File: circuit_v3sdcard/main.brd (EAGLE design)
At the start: 21.7 x 29.5 mm, 18 parts, among them CN1 SD, CN3 MICROSD, CN4 5035481020, IC1 C8051F381-GM, IC3 N25Q512A, IC4 KC2016K, IC6 MPU-9250

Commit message: Fix parts positions
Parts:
- added C1: 1.0u, reg,cap:1005
- added R3: 100, reg,cap:1005
- moved IC1 36.7 mm to (4.96, 20.1)
- moved C6 36.4 mm to (0.62, 19.6), turned to 270 degrees
- moved C9 15.4 mm to (16.6, 23.3), turned to 0 degrees
- moved D4 13.1 mm to (1.82, 13.8)
- moved C3 12.3 mm to (5.83, 13.4)
- moved C2 12.3 mm to (8.33, 13.4)
- moved C4 12.3 mm to (4.33, 12.6)
- moved IC6 12.3 mm to (6.83, 10.1)
- moved R26 11.0 mm to (14.1, 23.3), turned to 180 degrees
- moved R2 9.85 mm to (3.51, 6.00)
- moved IC3 8.15 mm to (13.6, 19.8), turned to 0 degrees
- moved C10 2.18 mm to (19.8, 21.7), turned to 0 degrees
- moved IC4 1.78 mm to (19.7, 19.1)
- moved R1 1.67 mm to (7.44, 1.29), turned to 90 degrees
- moved D3 0.55 mm to (1.61, 9.61)
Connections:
- new net N$4: IC1.8, R3.P$1
- net DGND: now also C1.P$1
- net N$1: now also C1.P$2
- net VBUS: now also R3.P$2; no longer IC1.8
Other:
- outline, holes or cut-outs redrawn

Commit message: Added wiring
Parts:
- moved C2 6.15 mm to (4.92, 8.24), turned to 0 degrees
- moved C4 6.03 mm to (9.05, 8.81), turned to 90 degrees
- moved C3 5.93 mm to (7.74, 7.75), turned to 180 degrees
- moved C6 3.42 mm to (2.29, 16.6), turned to 90 degrees
- moved R1 2.72 mm to (7.43, 4.00)
- moved IC6 1.50 mm to (6.83, 11.6), turned to 0 degrees
- moved C1 1.19 mm to (1.28, 16.6)
- moved R2 0.46 mm to (3.05, 5.96)
- moved C9 0.13 mm to (16.7, 23.3)
- moved R26 0.13 mm to (14.2, 23.3), turned to 0 degrees
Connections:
- net D+: now also CN4.4; no longer CN4.6
- net D-: now also CN4.6; no longer CN4.4
- net GPIO0: now also IC1.12; no longer IC1.26
- net GPIO1: now also IC1.11; no longer IC1.25
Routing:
- net DGND: track 1.98 -> 132.2 mm, vias 0 -> 19
- net +3V3: track 1.54 -> 68.3 mm, vias 0 -> 9
- net N$11: track 0.00 -> 34.2 mm, vias 0 -> 2
- net D+: track 0.00 -> 31.9 mm
- net TX1: track 0.00 -> 31.6 mm, vias 0 -> 2
- net RX1: track 0.00 -> 31.3 mm, vias 0 -> 2
- net D-: track 0.00 -> 30.5 mm
- net N$2: track 0.00 -> 28.6 mm, vias 0 -> 1
- net N$14: track 0.00 -> 27.1 mm, vias 0 -> 1
- net EEPROM_MOSI: track 0.00 -> 26.5 mm
- net EEPROM_SCK: track 0.00 -> 26.3 mm
- net C2D: track 0.00 -> 23.4 mm, vias 0 -> 2
- net C2CK: track 0.00 -> 23.3 mm, vias 0 -> 3
- net N$3: track 0.00 -> 21.4 mm, vias 0 -> 1
- net GPIO1: track 0.00 -> 20.6 mm, vias 0 -> 1
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
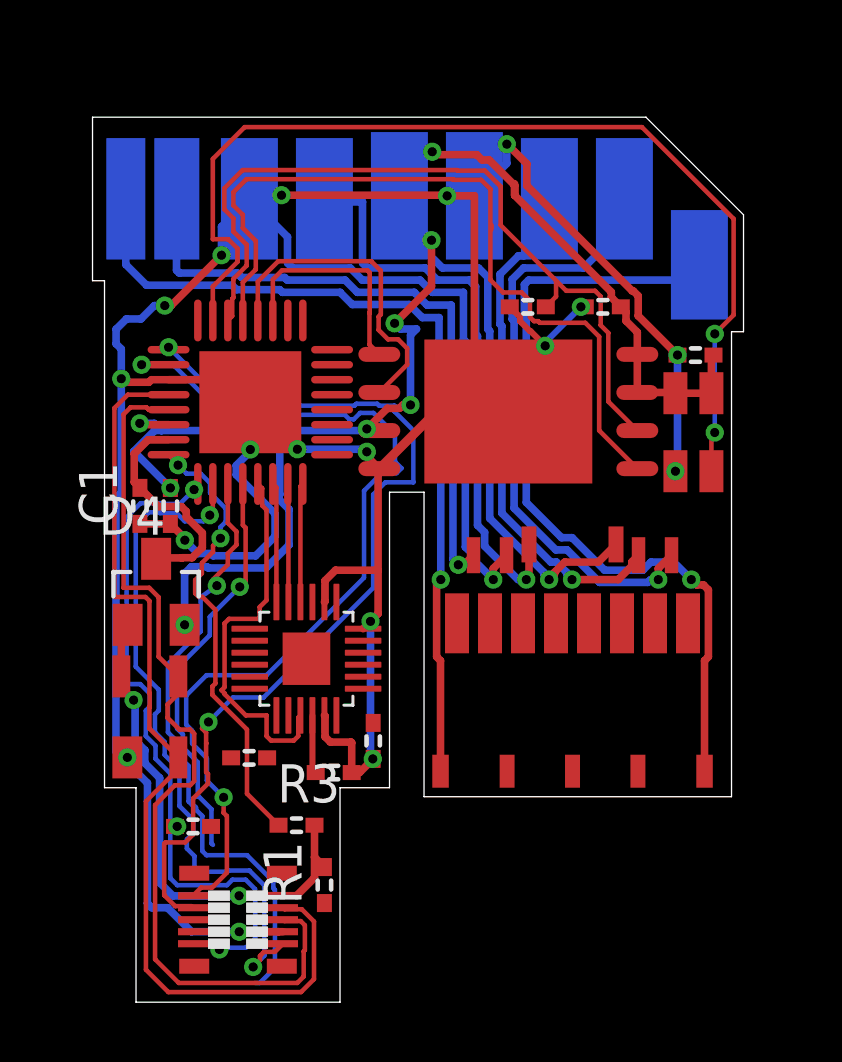
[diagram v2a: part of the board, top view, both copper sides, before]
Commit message: Connected air wires
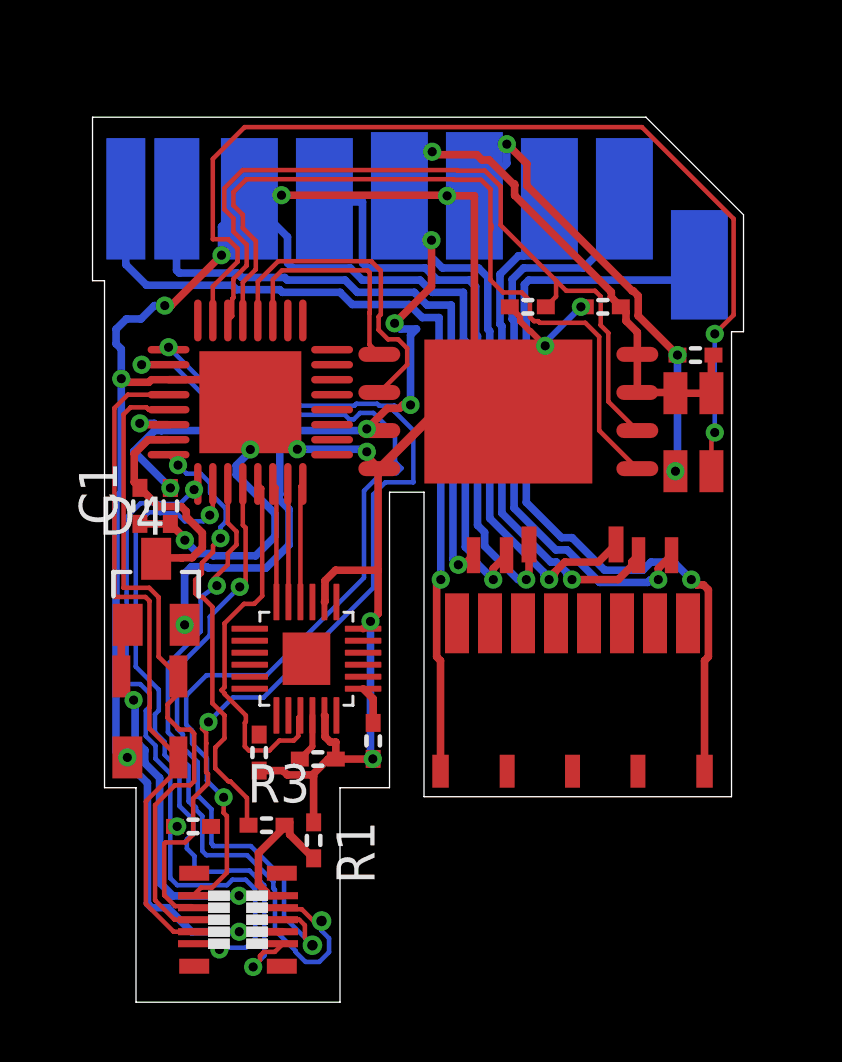
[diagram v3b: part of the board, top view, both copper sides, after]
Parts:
- moved R1 1.53 mm to (7.07, 5.50), turned to 270 degrees
- moved R3 1.00 mm to (5.50, 6.00)
- moved C3 0.70 mm to (7.21, 8.21)
- moved C2 0.38 mm to (5.25, 8.42), turned to 90 degrees
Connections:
- net D+: now also CN4.7; no longer CN4.4
- net D-: now also CN4.5; no longer CN4.6
- net GPIO0: now also CN4.6; no longer CN4.5
- net GPIO1: now also CN4.4; no longer CN4.7
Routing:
- net D+: track 31.9 -> 22.4 mm
- net D-: track 30.5 -> 22.2 mm
- net GPIO0: track 13.5 -> 20.6 mm, vias 1 -> 2
- net GPIO1: track 20.6 -> 23.5 mm, vias 1 -> 2
- net DGND: track 132.2 -> 135.0 mm
- net +3V3: track 68.3 -> 69.5 mm
- net VBUS: track 17.1 -> 18.1 mm

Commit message: Modified circuit
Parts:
- moved C2 0.50 mm to (4.75, 8.42)
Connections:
- net D+: now also CN4.5; no longer CN4.7
- net D-: now also CN4.3; no longer CN4.5
- net DGND: now also CN4.7; no longer CN4.8
- net GPIO0: now also CN4.8; no longer CN4.6
- net GPIO1: now also CN4.6; no longer CN4.4
- net RX1: now also CN4.4; no longer CN4.3
- net TX1: now also CN4.2; no longer CN4.1
- net VBUS: now also CN4.1; no longer CN4.2
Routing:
- net +3V3: track 69.5 -> 61.9 mm
- net DGND: track 135.0 -> 128.3 mm
- net C2D: track 23.4 -> 17.4 mm
- net N$4: track 14.9 -> 20.6 mm
- net TX1: track 31.6 -> 28.5 mm
- net RX1: track 31.3 -> 29.3 mm
- net GPIO1: track 23.5 -> 25.4 mm
- net GPIO0: track 20.6 -> 22.2 mm
- net VBUS: track 18.1 -> 17.6 mm
- net IMU_MISO: track 12.7 -> 13.2 mm, vias 0 -> 2

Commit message: No air wire
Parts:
- moved C4 0.57 mm to (8.59, 9.13)
- moved C2 0.50 mm to (4.75, 8.92)
- moved IC6 0.50 mm to (6.83, 12.1)
- moved R3 0.25 mm to (5.55, 6.25), turned to 180 degrees
- moved C3 0.13 mm to (7.14, 8.31)
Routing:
- net +3V3: track 61.9 -> 88.0 mm, vias 9 -> 10
- net N$4: track 20.6 -> 17.7 mm
- net C2D: track 17.4 -> 19.6 mm
- net DGND: track 128.3 -> 126.6 mm
- net RX1: track 29.3 -> 27.6 mm
- net IMU_MISO: track 13.2 -> 12.1 mm
- net TX1: track 28.5 -> 27.5 mm
- net C2CK: track 23.3 -> 22.4 mm, vias 3 -> 4
- net IMU_SCK: track 3.94 -> 3.44 mm
- net IMU_MOSI: track 3.98 -> 3.48 mm
- net IMU_!CS: track 3.97 -> 3.47 mm
- removed copper zone on layer 1, net +3V3

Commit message: Modified circuit
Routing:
- net GPIO1: track 24.9 -> 22.1 mm
- net GPIO0: track 22.2 -> 19.7 mm
- net N$4: track 17.7 -> 15.3 mm
- net N$11: track 34.2 -> 32.1 mm
- net +3V3: track 88.0 -> 86.4 mm
- net EEPROM_MOSI: track 26.3 -> 25.2 mm
- net EEPROM_SCK: track 26.3 -> 25.1 mm
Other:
- board text added: "Yoshiaki Sato"
- board text added: "virtualGimbal v3"
- board text removed: "Y. Sato"
- board text removed: "virtualGimbal"

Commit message: Modified parts values
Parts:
- D4: value HSMS-2854 -> BAT54CL
- IC3: value N25Q512A -> MT29F2G01ABAGDWB
- IC4: value KC2016K -> KC2016K48.0000C1GE00
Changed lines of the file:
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@@
 <layer number="21" name="tPlace" color="7" fill="1" visible="yes" active="yes"/>
 <layer number="22" name="bPlace" color="7" fill="1" visible="yes" active="yes"/>
-<layer number="23" name="tOrigins" color="15" fill="1" visible="no" active="yes"/>
-<layer number="24" name="bOrigins" color="15" fill="1" visible="no" active="yes"/>
+<layer number="23" name="tOrigins" color="15" fill="1" visible="yes" active="yes"/>
+<layer number="24" name="bOrigins" color="15" fill="1" visible="yes" active="yes"/>
 <layer number="25" name="tNames" color="7" fill="1" visible="no" active="yes"/>
 <layer number="26" name="bNames" color="7" fill="1" visible="no" active="yes"/>
@@
 <attribute name="VALUE" x="4.2001" y="16.0064" size="1.27" layer="27" rot="R90"/>
 </element>
-<element name="IC3" library="EEPROM" package="V-PDFN-8" value="N25Q512A" x="13.56" y="19.79">
+<element name="IC3" library="EEPROM" package="V-PDFN-8" value="MT29F2G01ABAGDWB" x="13.56" y="19.79">
 <attribute name="VALUE" x="9.925" y="15.79" size="0.8128" layer="27"/>
 </element>
@@
 <attribute name="VALUE" x="16.075" y="21.375" size="1.27" layer="27"/>
 </element>
-<element name="IC4" library="Oscillator" package="KC2016K" value="KC2016K" x="19.73" y="19.1" rot="R270">
+<element name="IC4" library="Oscillator" package="KC2016K" value="KC2016K48.0000C1GE00" x="19.73" y="19.1" rot="R270">
 <attribute name="VALUE" x="17.252" y="15.452" size="1.27" layer="27" ratio="10"/>
 </element>
@@
 <attribute name="VALUE" x="5.165" y="6.13" size="1.27" layer="27" rot="R270"/>
 </element>
-<element name="D4" library="avago" library_urn="urn:adsk.eagle:library:107" package="SOT23" package3d_urn="urn:adsk.eagle:package:4488/1" value="HSMS-2854" x="1.82" y="13.78">
+<element name="D4" library="avago" library_urn="urn:adsk.eagle:library:107" package="SOT23" package3d_urn="urn:adsk.eagle:package:4488/1" value="BAT54CL" x="1.82" y="13.78">
 <attribute name="NAME" x="-0.085" y="15.685" size="1.27" layer="25"/>
 <attribute name="VALUE" x="-0.085" y="10.605" size="1.27" layer="27"/>

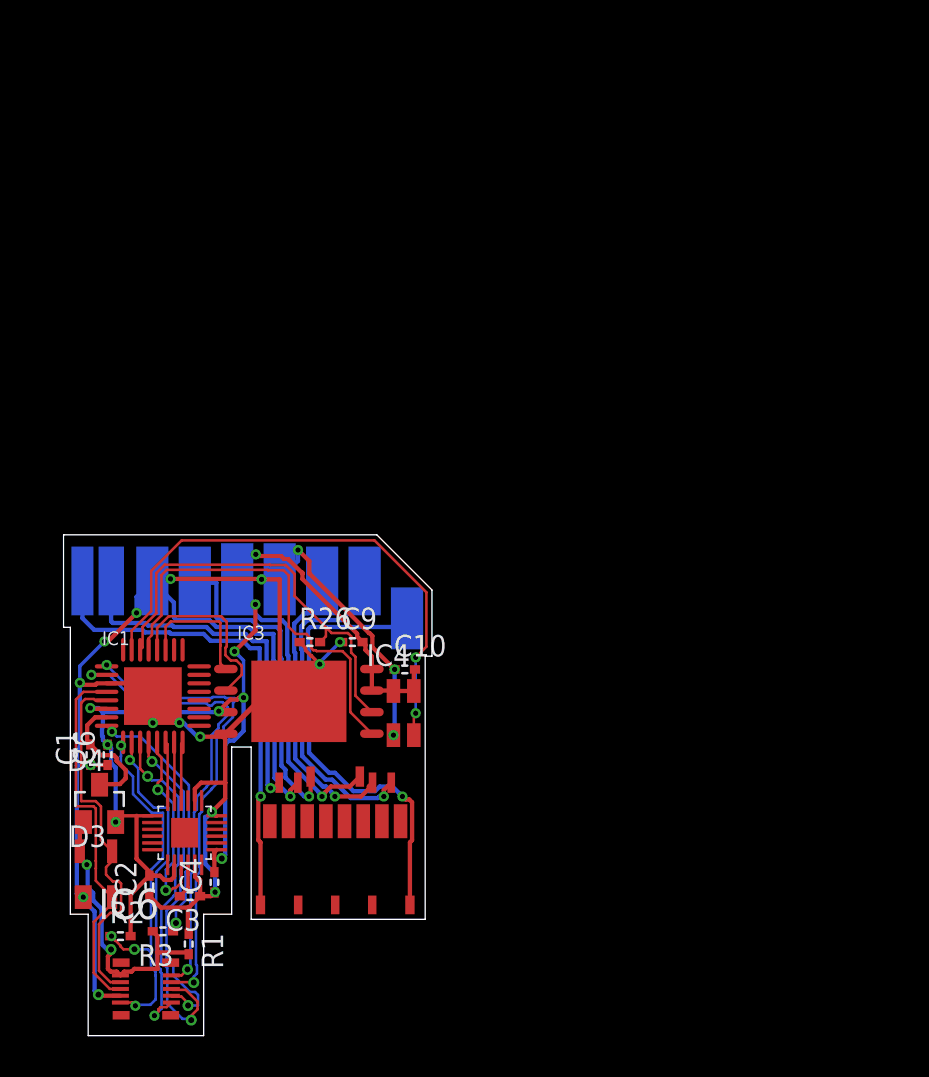
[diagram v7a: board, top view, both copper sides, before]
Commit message: Modifing sdcard circuit
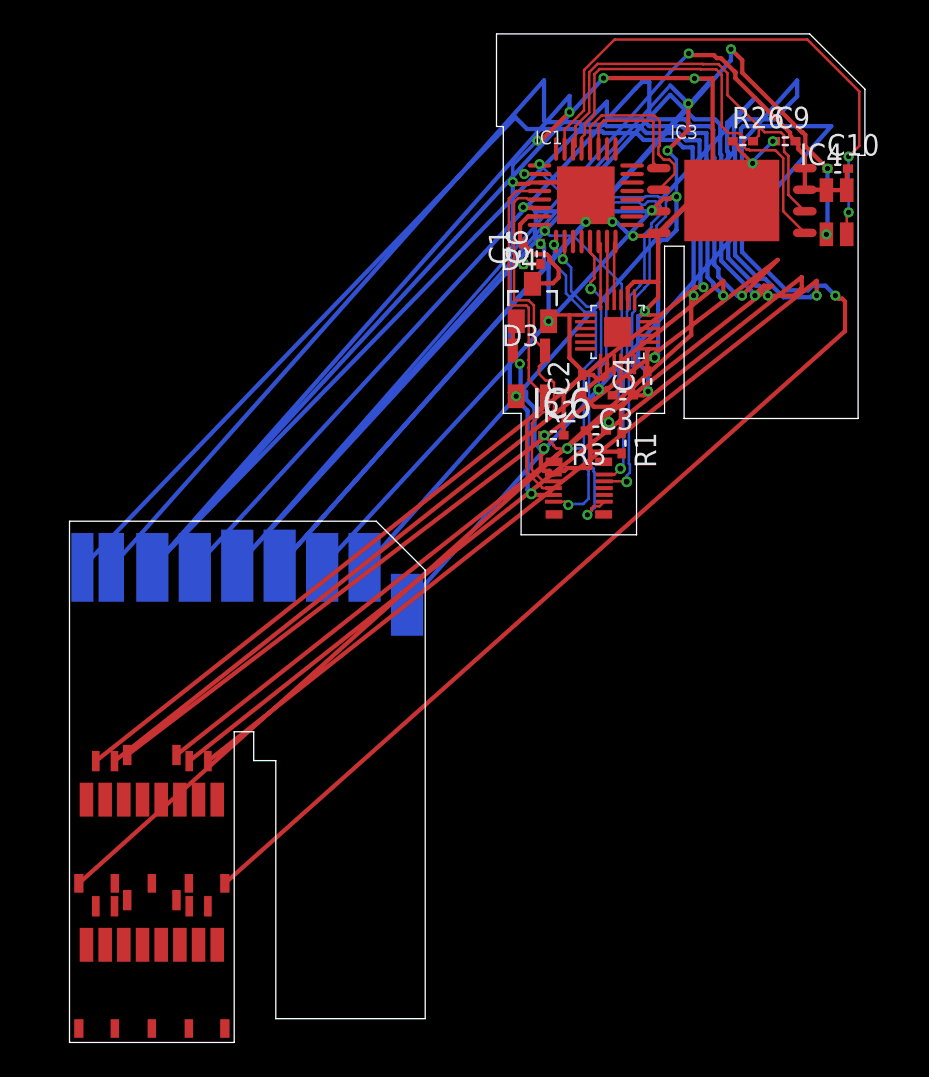
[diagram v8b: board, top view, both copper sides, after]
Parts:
- added CN2: (no value), Connector:BLOCK_SD_CONNECTOR
- CN3: value MICROSD -> (none)
- moved C1 39.0 mm to (26.8, 46.1)
- moved C2 39.0 mm to (30.3, 38.4)
- moved C3 39.0 mm to (32.6, 37.8)
- moved C4 39.0 mm to (34.1, 38.6)
- moved C9 39.0 mm to (42.2, 52.8)
- moved CN4 39.0 mm to (30.1, 32.4)
- moved D3 39.0 mm to (27.1, 39.1)
- moved D4 39.0 mm to (27.3, 43.3)
- moved IC1 39.0 mm to (30.5, 49.6)
- moved IC3 39.0 mm to (39.1, 49.3)
- moved R2 39.0 mm to (28.6, 35.5)
- moved R26 39.0 mm to (39.7, 52.8)
- moved C10 39.0 mm to (45.3, 51.2)
- moved C6 39.0 mm to (27.8, 46.1)
- moved IC4 39.0 mm to (45.2, 48.6)
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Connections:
- removed net GPIO0: CN4.8, IC1.12
- removed net GPIO1: CN4.6, IC1.11
- net +3V3: now also CN3.4; no longer CN3.VDD
- net C2CK: now also CN2.1
- net C2D: now also CN2.2
- net D+: now also CN2.7
- net D-: now also CN2.6
- net DGND: now also CN2.8, CN3.6; no longer CN3.VSS
- net N$10: now also CN3.3; no longer CN3.CMD
- net N$12: now also CN3.2; no longer CN3.CD/DAT3
- net N$14: now also CN3.1; no longer CN3.DAT2
- net N$2: now also CN3.8; no longer CN3.DAT1
- net N$3: now also CN3.7; no longer CN3.DAT0
- net N$6: now also CN3.5; no longer CN3.CLK
- net RX1: now also CN2.3
- net TX1: now also CN2.4
- net VBUS: now also CN2.5
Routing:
- net DGND: track 126.1 -> 358.5 mm
- net +3V3: track 86.4 -> 242.3 mm
- net N$6: track 19.6 -> 107.3 mm
- net N$12: track 20.0 -> 103.9 mm
- net N$3: track 21.4 -> 104.6 mm
- net N$10: track 17.3 -> 100.0 mm
- net N$14: track 27.1 -> 108.6 mm
- net N$2: track 28.6 -> 107.5 mm
- net GPIO1: track 22.1 -> 0.00 mm, vias 2 -> 0
- net GPIO0: track 19.7 -> 0.00 mm, vias 2 -> 0
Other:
- board size 21.7 x 29.5 mm -> 46.9 x 59.4 mm
